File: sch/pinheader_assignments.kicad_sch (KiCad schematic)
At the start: 1 part

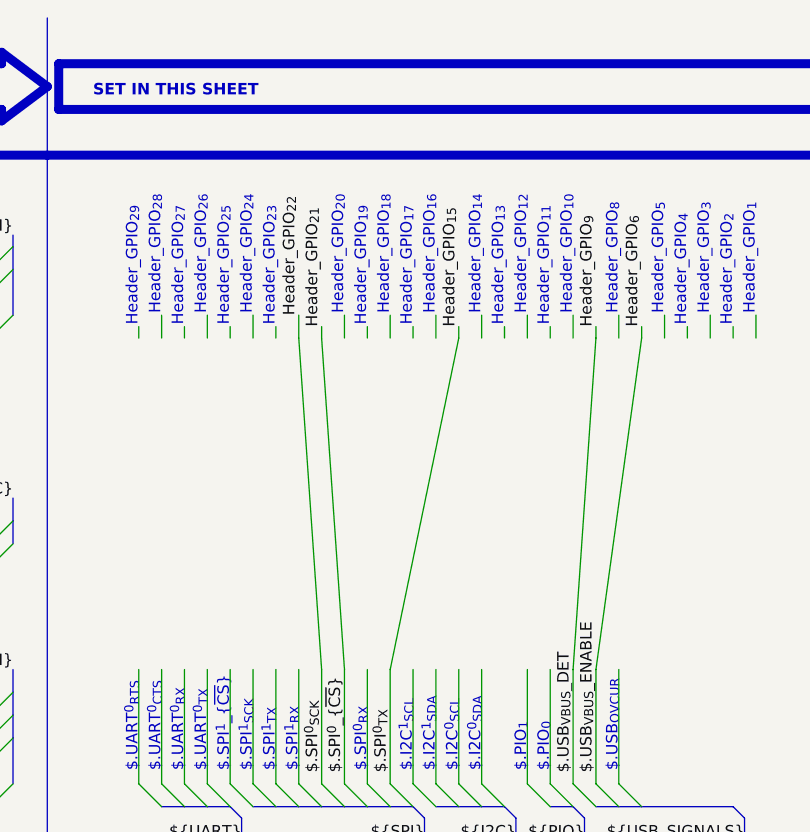
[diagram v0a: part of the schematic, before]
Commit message: Fixed pin assignments
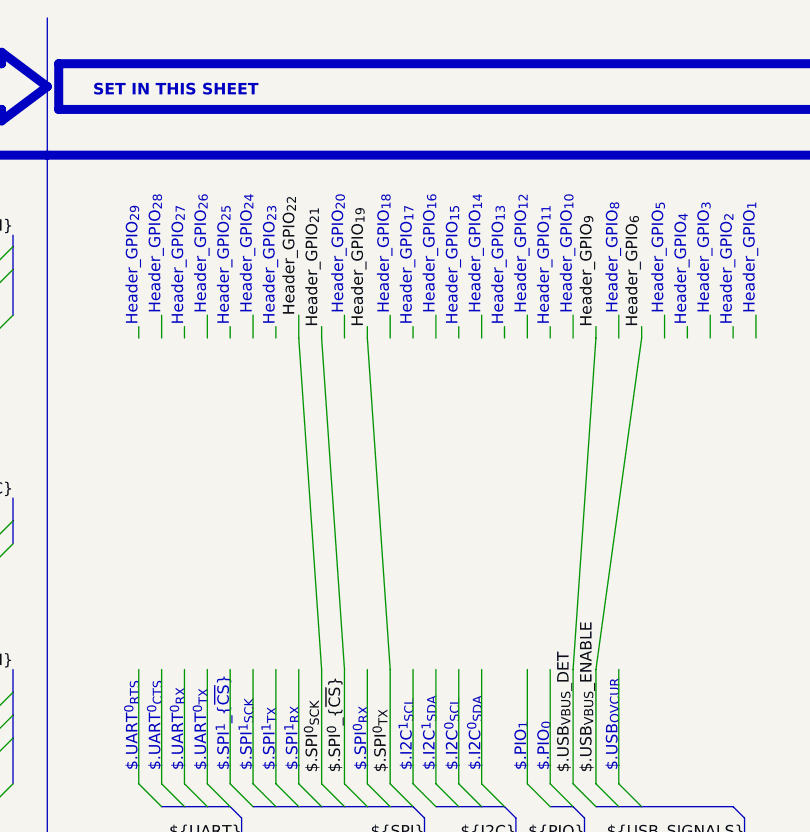
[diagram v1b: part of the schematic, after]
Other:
- note added: "Header_GPIO_{15}"
- note removed: "Header_GPIO_{19}"
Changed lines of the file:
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@@
 (kicad_sch (version 20211123) (generator eeschema)
   (paper "A4")
+  (bus_alias "BTN" (members "A" "B" "UP" "DOWN" "LEFT" "RIGHT" "START" "SELECT"))
+  (bus_alias "UART" (members "UART^{0}_{TX}" "UART^{0}_{RX}" "UART^{0}_{CTS}" "UART^{0}_{RTS}" "UART^{1}_{TX}" "UART^{1}_{RX}" "UART^{1}_{CTS}" "UART^{1}_{RTS}"))
+  (bus_alias "USB_SIGNALS" (members "USB_{OVCUR}" "USB_{VBUS}_ENABLE" "USB_{VBUS}_DET"))
+  (bus_alias "SPI" (members "SPI^{0}_{RX}" "SPI^{0}_{~{CS}}" "SPI^{0}_{SCK}" "SPI^{1}_{RX}" "SPI^{1}_{~{CS}}" "SPI^{1}_{SCK}" "SPI^{0}_{TX}" "SPI^{1}_{TX}"))
+  (bus_alias "ADC" (members "ADC_{0}" "ADC_{1}" "ADC_{2}" "ADC_{3}"))
+  (bus_alias "PIO" (members "PIO_{0}" "PIO_{1}"))
+  (bus_alias "PWM" (members "PWM_{0}^{A}" "PWM_{0}^{B}" "PWM_{1}^{A}" "PWM_{2}^{A}" "PWM_{3}^{A}" "PWM_{4}^{A}" "PWM_{5}^{A}" "PWM_{6}^{A}" "PWM_{1}^{B}" "PWM_{2}^{B}" "PWM_{3}^{B}" "PWM_{4}^{B}" "PWM_{5}^{B}" "PWM_{6}^{B}"))
+  (bus_alias "GPIO" (members "GPIO_{1}" "GPIO_{2}" "GPIO_{3}" "GPIO_{4}" "GPIO_{5}" "GPIO_{6}" "GPIO_{7}" "GPIO_{8}" "GPIO_{9}" "GPIO_{10}" "GPIO_{11}" "GPIO_{12}" "GPIO_{13}" "GPIO_{14}" "GPIO_{15}" "GPIO_{16}" "GPIO_{17}" "GPIO_{18}" "GPIO_{19}" "GPIO_{20}" "GPIO_{21}" "GPIO_{22}" "GPIO_{23}" "GPIO_{24}" "GPIO_{25}" "GPIO_{26}" "GPIO_{27}" "GPIO_{28}" "GPIO_{29}"))
+  (bus_alias "CLOCK" (members "GPIN_{0}" "GPOUT_{0}" "GPIN_{1}" "GPOUT_{1}" "GPOUT_{2}" "GPOUT_{3}"))
   (bus_alias "I2C" (members "I2C^{0}_{SDA}" "I2C^{0}_{SCL}" "I2C^{1}_{SDA}" "I2C^{1}_{SCL}"))
-  (bus_alias "PWM" (members "PWM_{0}^{A}" "PWM_{0}^{B}" "PWM_{1}^{A}" "PWM_{2}^{A}" "PWM_{3}^{A}" "PWM_{4}^{A}" "PWM_{5}^{A}" "PWM_{6}^{A}" "PWM_{1}^{B}" "PWM_{2}^{B}" "PWM_{3}^{B}" "PWM_{4}^{B}" "PWM_{5}^{B}" "PWM_{6}^{B}"))
-  (bus_alias "PIO" (members "PIO_{0}" "PIO_{1}"))
-  (bus_alias "ADC" (members "ADC_{0}" "ADC_{1}" "ADC_{2}" "ADC_{3}"))
-  (bus_alias "CLOCK" (members "GPIN_{0}" "GPOUT_{0}" "GPIN_{1}" "GPOUT_{1}" "GPOUT_{2}" "GPOUT_{3}"))
-  (bus_alias "SPI" (members "SPI^{0}_{RX}" "SPI^{0}_{~{CS}}" "SPI^{0}_{SCK}" "SPI^{1}_{RX}" "SPI^{1}_{~{CS}}" "SPI^{1}_{SCK}" "SPI^{0}_{TX}" "SPI^{1}_{TX}"))
-  (bus_alias "GPIO" (members "GPIO_{1}" "GPIO_{2}" "GPIO_{3}" "GPIO_{4}" "GPIO_{5}" "GPIO_{6}" "GPIO_{7}" "GPIO_{8}" "GPIO_{9}" "GPIO_{10}" "GPIO_{11}" "GPIO_{12}" "GPIO_{13}" "GPIO_{14}" "GPIO_{15}" "GPIO_{16}" "GPIO_{17}" "GPIO_{18}" "GPIO_{19}" "GPIO_{20}" "GPIO_{21}" "GPIO_{22}" "GPIO_{23}" "GPIO_{24}" "GPIO_{25}" "GPIO_{26}" "GPIO_{27}" "GPIO_{28}" "GPIO_{29}"))
-  (bus_alias "USB_SIGNALS" (members "USB_{OVCUR}" "USB_{VBUS}_ENABLE" "USB_{VBUS}_DET"))
-  (bus_alias "UART" (members "UART^{0}_{TX}" "UART^{0}_{RX}" "UART^{0}_{CTS}" "UART^{0}_{RTS}" "UART^{1}_{TX}" "UART^{1}_{RX}" "UART^{1}_{CTS}" "UART^{1}_{RTS}"))
-  (bus_alias "BTN" (members "A" "B" "UP" "DOWN" "LEFT" "RIGHT" "START" "SELECT"))
   (bus_entry (at 152.4 176.53) (size 2.54 -2.54)
     (stroke (width 0) (type default) (color 0 0 0 0))
@@
     (stroke (width 0) (type default) (color 0 0 0 0))
   )
+  (wire (pts (xy 118.11 34.29) (xy 120.65 71.12))
+    (stroke (width 0) (type default) (color 0 0 0 0))
+  )
   (wire (pts (xy 132.08 143.51) (xy 132.08 173.99))
     (stroke (width 0) (type default) (color 0 0 0 0))
@@
   )
   (bus (pts (xy 234.95 17.78) (xy 237.49 20.32))
-    (stroke (width 0) (type default) (color 0 0 0 0))
-  )
-  (wire (pts (xy 120.65 71.12) (xy 128.27 34.29))
     (stroke (width 0) (type default) (color 0 0 0 0))
   )
@@
     (effects (font (size 1.27 1.27)) (justify right bottom))
   )
-  (text "Header_GPIO_{19}" (at 118.11 33.02 90)
+  (text "Header_GPIO_{15}" (at 128.27 33.02 90)
     (effects (font (size 1.27 1.27)) (justify left bottom))
   )
@@
     (effects (font (size 1.27 1.27)) (justify left bottom))
   )
-  (label "Header_GPIO_{15}" (at 128.27 33.02 90)
-    (effects (font (size 1.27 1.27)) (justify left bottom))
-  )
   (label "Header_GPIO_{5}" (at 50.8 81.28 0)
     (effects (font (size 1.27 1.27)) (justify left bottom))
@@
     (effects (font (size 1.27 1.27)) (justify left bottom))
   )
+  (label "Header_GPIO_{19}" (at 118.11 33.02 90)
+    (effects (font (size 1.27 1.27)) (justify left bottom))
+  )

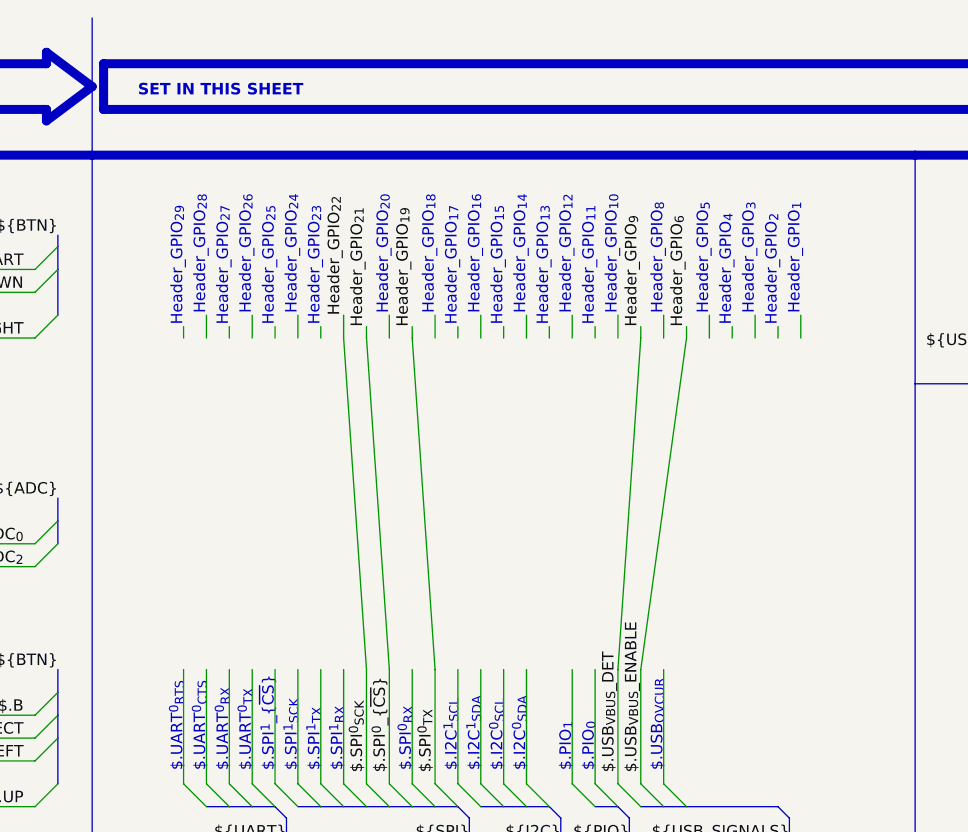
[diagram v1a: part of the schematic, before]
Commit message: Fixed SPI pin assignments to SPI0 only
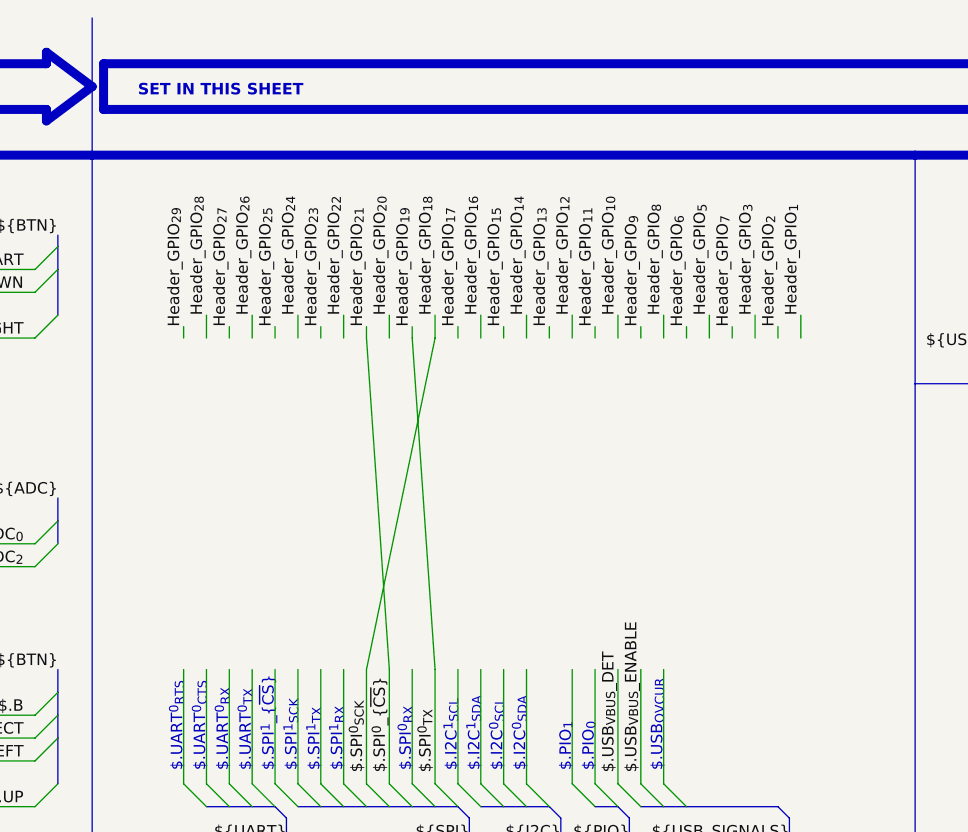
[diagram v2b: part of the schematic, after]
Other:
- note removed: "Header_GPIO_{10}"
- note removed: "Header_GPIO_{11}"
- note removed: "Header_GPIO_{12}"
- note removed: "Header_GPIO_{13}"
- note removed: "Header_GPIO_{14}"
- note removed: "Header_GPIO_{15}"
- note removed: "Header_GPIO_{16}"
- note removed: "Header_GPIO_{17}"
- note removed: "Header_GPIO_{18}"
- note removed: "Header_GPIO_{1}"
- note removed: "Header_GPIO_{20}"
- note removed: "Header_GPIO_{23}"
- note removed: "Header_GPIO_{24}"
- note removed: "Header_GPIO_{25}"
- note removed: "Header_GPIO_{26}"
- note removed: "Header_GPIO_{27}"
- note removed: "Header_GPIO_{28}"
- note removed: "Header_GPIO_{29}"
- note removed: "Header_GPIO_{2}"
- note removed: "Header_GPIO_{3}"
- note removed: "Header_GPIO_{4}"
- note removed: "Header_GPIO_{5}"
- note removed: "Header_GPIO_{8}"
